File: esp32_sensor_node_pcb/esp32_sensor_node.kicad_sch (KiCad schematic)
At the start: 28 parts, among them J1 Conn_02x10_Odd_Even, Q1 2N7002K, SW1 SW_DIP_x01, SW2 SW_DIP_x01, U1 HT7833, U2 ESP32-WROOM-E, U3 MAX3483AEASA+

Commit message: Changed schematic - 3.3V to RS485, 5V to Soil sensor. Changed resistor from 1.9k to 4.7k. Finished routing of PCB with new schematic
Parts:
- R2: value 1.91K -> 4.7K
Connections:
- net +3.3V: no longer JST_XH_SOIL5V1.1 (Pin_1)
- net +5V: now also JST_XH_SOIL5V1.1 (Pin_1)
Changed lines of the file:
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@@
   (junction (at 224.79 128.27) (diameter 0) (color 0 0 0 0)
   )
-  (junction (at 207.01 46.99) (diameter 0) (color 0 0 0 0)
-  )
   (junction (at 224.79 113.03) (diameter 0) (color 0 0 0 0)
   )
@@
     (stroke (width 0) (type default))
   )
-  (wire (pts (xy 207.01 46.99) (xy 218.44 46.99))
-    (stroke (width 0) (type default))
-  )
   (wire (pts (xy 224.79 123.19) (xy 224.79 125.73))
     (stroke (width 0) (type default))
@@
   )
   (wire (pts (xy 142.24 109.22) (xy 142.24 110.49))
+    (stroke (width 0) (type default))
+  )
+  (wire (pts (xy 210.82 44.45) (xy 210.82 46.99))
     (stroke (width 0) (type default))
   )
@@
     (stroke (width 0) (type dash))
   )
+  (wire (pts (xy 210.82 46.99) (xy 218.44 46.99))
+    (stroke (width 0) (type default))
+  )
   (wire (pts (xy 33.02 106.68) (xy 40.64 106.68))
     (stroke (width 0) (type default))
@@
     (stroke (width 0) (type default))
   )
-  (wire (pts (xy 200.66 46.99) (xy 207.01 46.99))
+  (wire (pts (xy 200.66 46.99) (xy 203.2 46.99))
     (stroke (width 0) (type default))
   )
@@
     (stroke (width 0) (type default))
   )
-  (wire (pts (xy 207.01 44.45) (xy 207.01 46.99))
+  (wire (pts (xy 203.2 44.45) (xy 203.2 46.99))
     (stroke (width 0) (type default))
   )
@@
     )
   )
-  (symbol (lib_id "power:+3.3V") (at 207.01 44.45 0) (unit 1)
-    (in_bom yes) (on_board yes) (dnp no) (fields_autoplaced)
-    (property "Reference" "#PWR014" (at 207.01 48.26 0)
-      (effects (font (size 1.27 1.27)) hide)
-    )
-    (property "Value" "+3.3V" (at 207.01 39.37 0)
-      (effects (font (size 1.27 1.27)))
-    )
-    (property "Footprint" "" (at 207.01 44.45 0)
-      (effects (font (size 1.27 1.27)) hide)
-    )
-    (property "Datasheet" "" (at 207.01 44.45 0)
+  (symbol (lib_id "power:+3.3V") (at 203.2 44.45 0) (unit 1)
+    (in_bom yes) (on_board yes) (dnp no) (fields_autoplaced)
+    (property "Reference" "#PWR014" (at 203.2 48.26 0)
+      (effects (font (size 1.27 1.27)) hide)
+    )
+    (property "Value" "+3.3V" (at 203.2 39.37 0)
+      (effects (font (size 1.27 1.27)))
+    )
+    (property "Footprint" "" (at 203.2 44.45 0)
+      (effects (font (size 1.27 1.27)) hide)
+    )
+    (property "Datasheet" "" (at 203.2 44.45 0)
       (effects (font (size 1.27 1.27)) hide)
     )
@@
         (path "/f305b47d-1a34-49f4-94a4-22a58fb9ed31"
           (reference "#PWR01") (unit 1)
+        )
+      )
+    )
+  )
+  (symbol (lib_id "power:+5V") (at 210.82 44.45 0) (unit 1)
+    (in_bom yes) (on_board yes) (dnp no) (fields_autoplaced)
+    (property "Reference" "#PWR024" (at 210.82 48.26 0)
+      (effects (font (size 1.27 1.27)) hide)
+    )
+    (property "Value" "+5V" (at 210.82 39.37 0)
+      (effects (font (size 1.27 1.27)))
+    )
+    (property "Footprint" "" (at 210.82 44.45 0)
+      (effects (font (size 1.27 1.27)) hide)
+    )
+    (property "Datasheet" "" (at 210.82 44.45 0)
+      (effects (font (size 1.27 1.27)) hide)
+    )
+    (pin "1")
+    (instances
+      (project "esp32_sensor_node"
+        (path "/f305b47d-1a34-49f4-94a4-22a58fb9ed31"
+          (reference "#PWR024") (unit 1)
         )
       )
@@
       (effects (font (size 1.27 1.27)) (justify right))
     )
-    (property "Value" "1.91K" (at 265.43 123.19 0)
+    (property "Value" "4.7K" (at 265.43 123.19 0)
       (effects (font (size 1.27 1.27)) (justify right))
     )

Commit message: Add transfer vias for all HSS, remove some routing voids, standardize track lengths for power and signal
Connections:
- net GPIO13: now also J1.1 (Pin_1); no longer J1.11 (Pin_11)
- net GPIO18: now also J1.3 (Pin_3); no longer J1.1 (Pin_1)
- net GPIO19: now also J1.5 (Pin_5); no longer J1.3 (Pin_3)
- net GPIO21: now also J1.7 (Pin_7); no longer J1.5 (Pin_5)
- net GPIO23: now also J1.9 (Pin_9); no longer J1.7 (Pin_7)
- net GPIO26: now also J1.11 (Pin_11); no longer J1.9 (Pin_9)
- net at U3.6 (A): now also JST_XH_SOIL5V1.2 (Pin_2); no longer JST_XH_SOIL5V1.3 (Pin_3)
- net at U3.7 (B): now also JST_XH_SOIL5V1.3 (Pin_3); no longer JST_XH_SOIL5V1.2 (Pin_2)

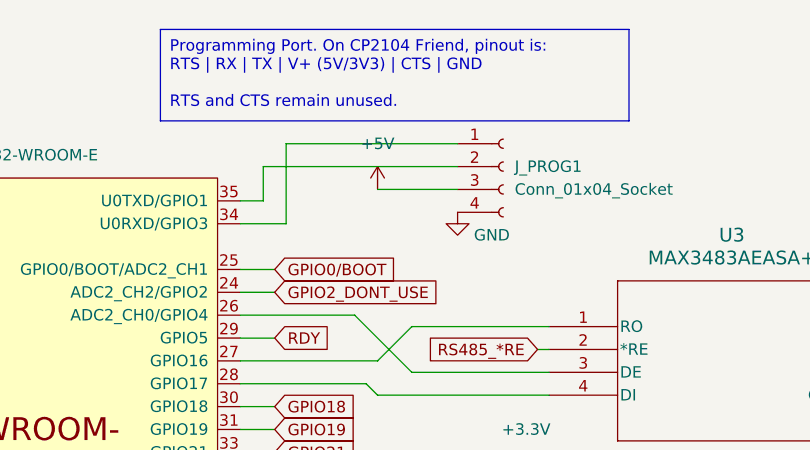
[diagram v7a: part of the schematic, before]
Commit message: Center MCU, reroute cleanup, add labels and shift components to fit
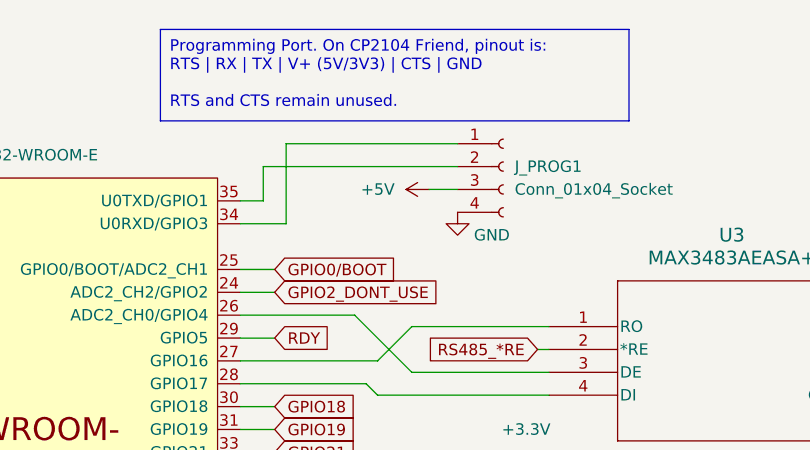
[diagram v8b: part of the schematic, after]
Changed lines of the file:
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@@
     (stroke (width 0) (type default))
   )
-  (wire (pts (xy 140.97 31.75) (xy 149.86 31.75))
+  (wire (pts (xy 146.685 31.75) (xy 149.86 31.75))
     (stroke (width 0) (type default))
   )
@@
     )
   )
-  (symbol (lib_id "power:+5V") (at 140.97 31.75 0) (unit 1)
+  (symbol (lib_id "power:+5V") (at 146.685 31.75 90) (unit 1)
     (in_bom yes) (on_board yes) (dnp no) (fields_autoplaced)
-    (property "Reference" "#PWR09" (at 140.97 35.56 0)
-      (effects (font (size 1.27 1.27)) hide)
-    )
-    (property "Value" "+5V" (at 140.97 26.67 0)
-      (effects (font (size 1.27 1.27)))
-    )
-    (property "Footprint" "" (at 140.97 31.75 0)
-      (effects (font (size 1.27 1.27)) hide)
-    )
-    (property "Datasheet" "" (at 140.97 31.75 0)
-      (effects (font (size 1.27 1.27)) hide)
-    )
+    (property "Reference" "#PWR09" (at 150.495 31.75 0)
+      (effects (font (size 1.27 1.27)) hide)
+    )
+    (property "Value" "+5V" (at 142.875 31.75 90)
+      (effects (font (size 1.27 1.27)) (justify left))
+    )
+    (property "Footprint" "" (at 146.685 31.75 0)
+      (effects (font (size 1.27 1.27)) hide)
+    )
+    (property "Datasheet" "" (at 146.685 31.75 0)
+      (effects (font (size 1.27 1.27)) hide)
+    )
